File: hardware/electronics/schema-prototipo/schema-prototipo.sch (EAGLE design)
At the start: 6 parts, among them IC1 7404N

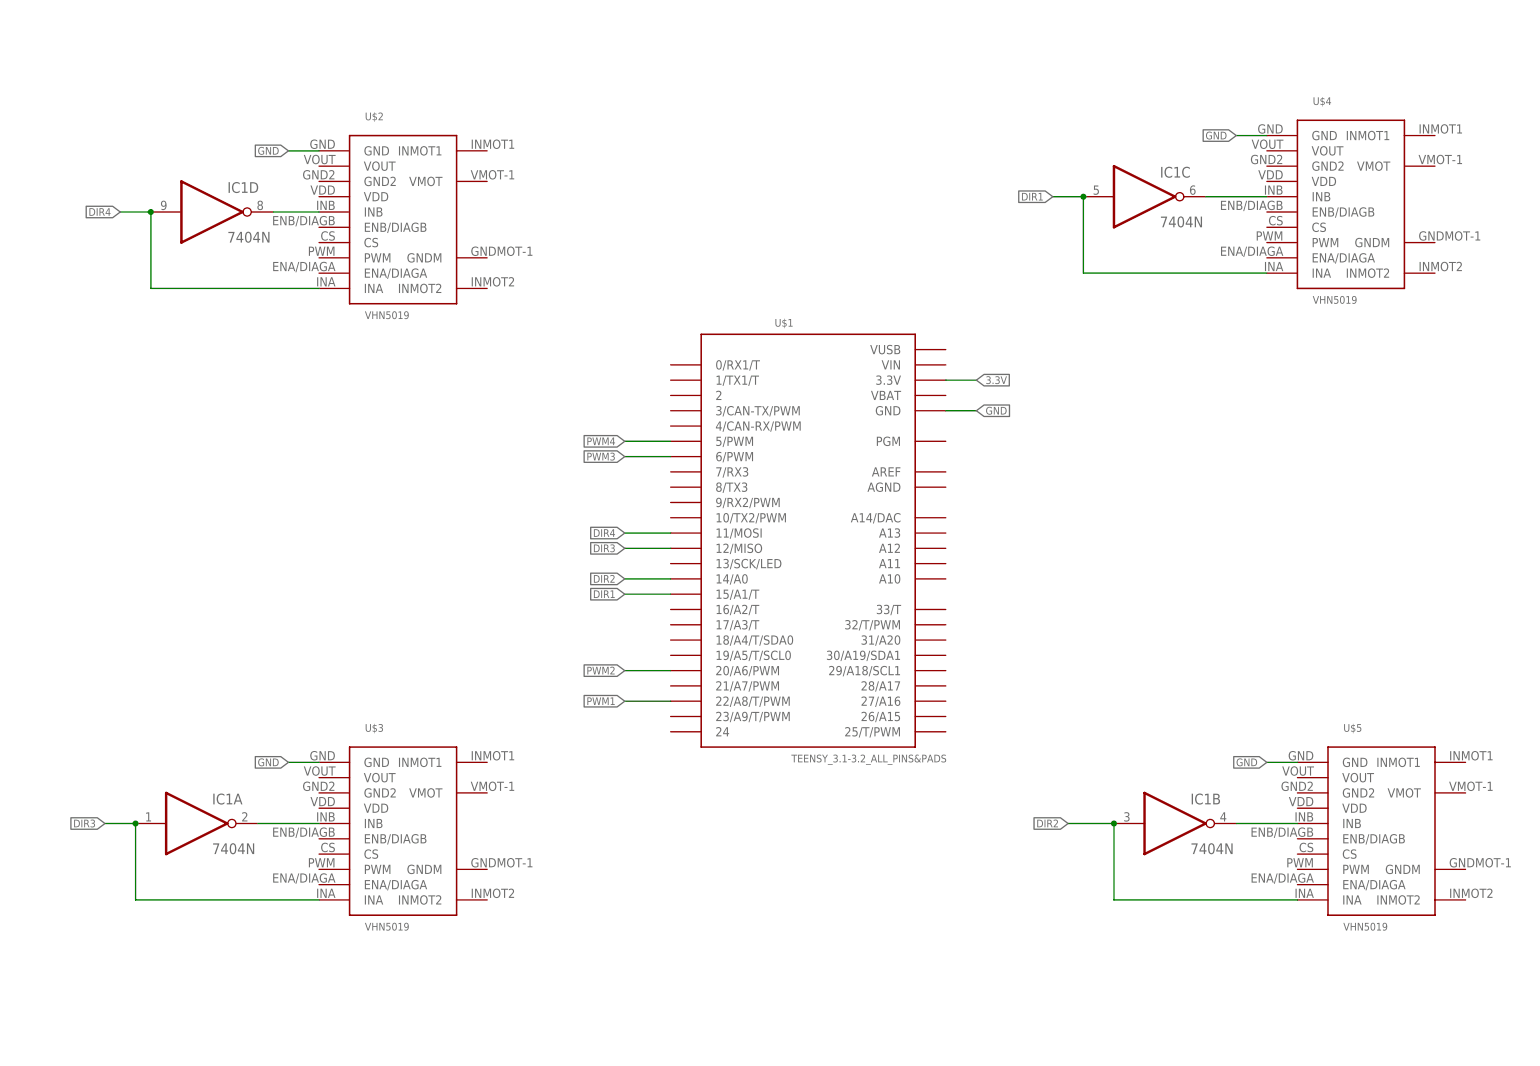
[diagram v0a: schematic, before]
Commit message: Fixed base schematic and board
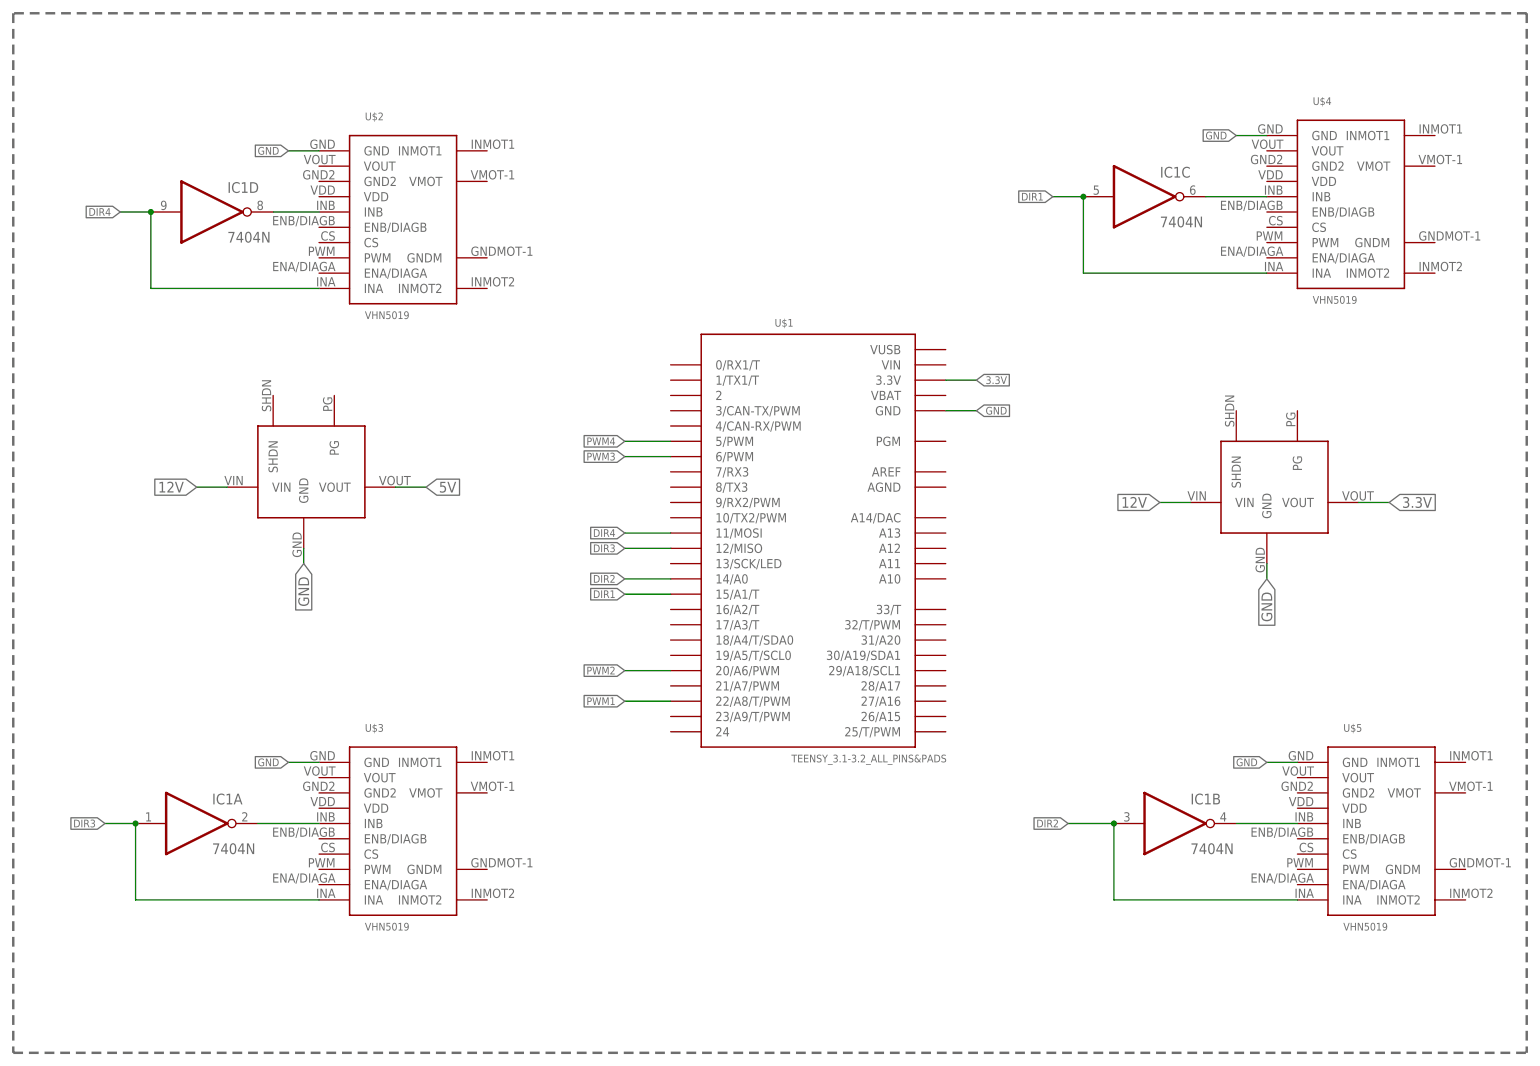
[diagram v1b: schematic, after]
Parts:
- added U$6, U$7: REGOLATORE-3.3V-1A, libreria valerio:REGOLATORE-3.3V-1A
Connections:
- new net 12V: U$6.VIN, U$7.VIN
- new net 5V: U$7.VOUT
- net 3.3V: now also U$6.VOUT
- net GND: now also U$6.GND, U$7.GND
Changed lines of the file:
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@@
 <part name="U$5" library="VHN5019" deviceset="VHN5019" device=""/>
 <part name="IC1" library="74xx-eu" library_urn="urn:adsk.eagle:library:85" deviceset="74*04" device="N" package3d_urn="urn:adsk.eagle:package:2008/1"/>
+<part name="U$6" library="libreria valerio" deviceset="REGOLATORE-3.3V-1A" device=""/>
+<part name="U$7" library="libreria valerio" deviceset="REGOLATORE-3.3V-1A" device=""/>
 </parts>
 <sheets>
 <sheet>
 <plain>
+<wire x1="223.52" y1="200.66" x2="-27.94" y2="200.66" width="0.4064" layer="96" style="longdash"/>
+<wire x1="-27.94" y1="200.66" x2="-27.94" y2="27.94" width="0.4064" layer="96" style="longdash"/>
+<wire x1="-27.94" y1="27.94" x2="223.52" y2="27.94" width="0.4064" layer="96" style="longdash"/>
+<wire x1="223.52" y1="200.66" x2="223.52" y2="27.94" width="0.4064" layer="96" style="longdash"/>
 </plain>
 <instances>
@@
 <instance part="IC1" gate="C" x="160.02" y="170.18"/>
 <instance part="IC1" gate="D" x="5.08" y="167.64"/>
+<instance part="U$6" gate="G$1" x="180.34" y="121.92"/>
+<instance part="U$7" gate="G$1" x="20.32" y="124.46"/>
 </instances>
 <busses>
@@
 <label x="17.78" y="76.2" size="1.27" layer="95" rot="R180" xref="yes"/>
 </segment>
+<segment>
+<pinref part="U$6" gate="G$1" pin="GND"/>
+<wire x1="180.34" y1="109.22" x2="180.34" y2="106.68" width="0.1524" layer="91"/>
+<label x="180.34" y="106.68" size="1.778" layer="95" rot="R270" xref="yes"/>
+</segment>
+<segment>
+<pinref part="U$7" gate="G$1" pin="GND"/>
+<wire x1="20.32" y1="111.76" x2="20.32" y2="109.22" width="0.1524" layer="91"/>
+<label x="20.32" y="109.22" size="1.778" layer="95" rot="R270" xref="yes"/>
+</segment>
 </net>
 <net name="3.3V" class="0">
@@
 <label x="132.08" y="139.7" size="1.27" layer="95" xref="yes"/>
 </segment>
-</net>
+<segment>
+<pinref part="U$6" gate="G$1" pin="VOUT"/>
+<wire x1="195.58" y1="119.38" x2="200.66" y2="119.38" width="0.1524" layer="91"/>
+<label x="200.66" y="119.38" size="1.778" layer="95" xref="yes"/>
+</segment>
+</net>
+<net name="12V" class="0">
+<segment>
+<pinref part="U$6" gate="G$1" pin="VIN"/>
+<wire x1="167.64" y1="119.38" x2="162.56" y2="119.38" width="0.1524" layer="91"/>
+<label x="162.56" y="119.38" size="1.778" layer="95" rot="R180" xref="yes"/>
+</segment>
+<segment>
+<pinref part="U$7" gate="G$1" pin="VIN"/>
+<wire x1="7.62" y1="121.92" x2="2.54" y2="121.92" width="0.1524" layer="91"/>
+<label x="2.54" y="121.92" size="1.778" layer="95" rot="R180" xref="yes"/>
+</segment>
+</net>
+<net name="5V" class="0">
+<segment>
+<pinref part="U$7" gate="G$1" pin="VOUT"/>
+<wire x1="35.56" y1="121.92" x2="40.64" y2="121.92" width="0.1524" layer="91"/>
+<label x="40.64" y="121.92" size="1.778" layer="95" xref="yes"/>
+</segment>
+</net>

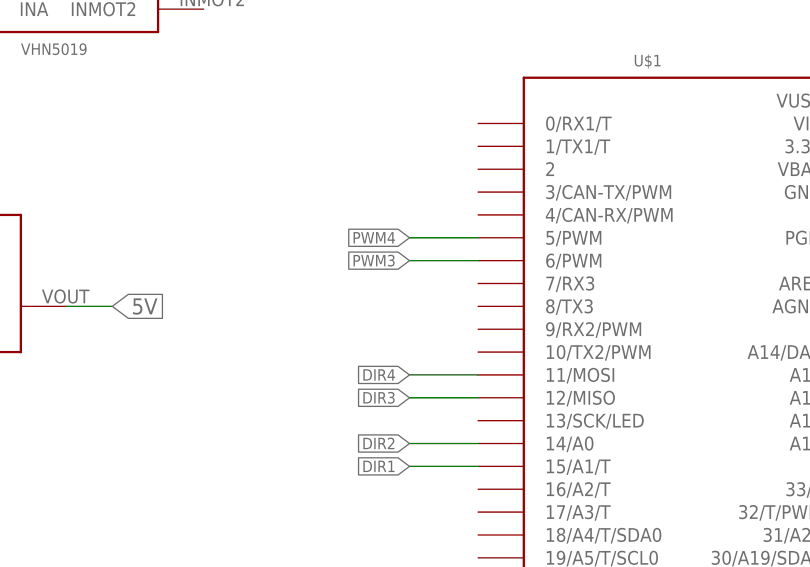
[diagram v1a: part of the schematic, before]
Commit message: Aggiornamento lib-motori
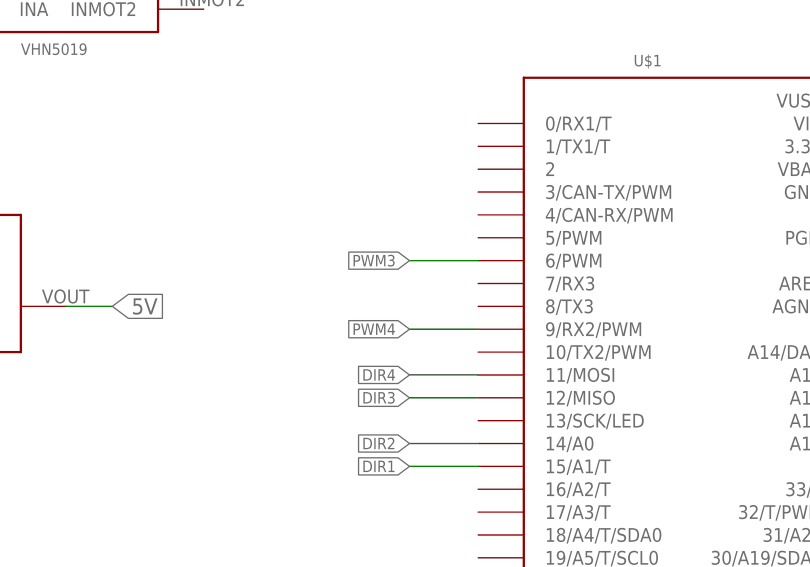
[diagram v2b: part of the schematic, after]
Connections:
- net PWM4: now also U$1.9/RX2/PWM; no longer U$1.5/PWM
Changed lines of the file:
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@@
 <?xml version="1.0" encoding="utf-8"?>
 <!DOCTYPE eagle SYSTEM "eagle.dtd">
-<eagle version="8.5.2">
+<eagle version="8.6.0">
 <drawing>
 <settings>
@@
 </segment>
 </net>
-<net name="PWM4" class="0">
-<segment>
-<pinref part="U$1" gate="G$1" pin="5/PWM"/>
-<wire x1="81.28" y1="129.54" x2="73.66" y2="129.54" width="0.1524" layer="91"/>
-<label x="73.66" y="129.54" size="1.27" layer="95" rot="R180" xref="yes"/>
-</segment>
-</net>
 <net name="PWM3" class="0">
 <segment>
@@
 </segment>
 </net>
+<net name="PWM4" class="0">
+<segment>
+<pinref part="U$1" gate="G$1" pin="9/RX2/PWM"/>
+<wire x1="81.28" y1="119.38" x2="73.66" y2="119.38" width="0.1524" layer="91"/>
+<label x="73.66" y="119.38" size="1.27" layer="95" rot="R180" xref="yes"/>
+</segment>
+</net>
